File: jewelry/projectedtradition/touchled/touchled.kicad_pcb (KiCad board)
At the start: 2 copper layers, 22 x 22 mm, 10 parts, among them J1 Conn_01x01, J2 Conn_01x01, J3 Conn_01x01, J4 Conn_01x01, U1 TPP223-BA6

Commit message: jewelry: Initial layout for touchled
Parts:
- removed D1: LED, LEDs:LED_1206_HandSoldering
- removed J4: Conn_01x01, Pin_Headers:Pin_Header_Straight_1x01_Pitch1.27mm
- added C3: 1uF, Capacitors_SMD:C_0805_HandSoldering, F.Cu at (-9.14, 2.79)
- added C4: 1uF, Capacitors_SMD:C_0805_HandSoldering, F.Cu at (-0.25, -10.9)
- added TP1: TEST, touchuc:progpin, F.Cu at (10.7, -2.29)
- added TP2: TEST, touchuc:progpin, F.Cu at (-6.60, -9.14)
- added TP3: TEST, touchuc:progpin, F.Cu at (4.06, -6.60)
- added U2: AP3019A, touchled:SOT-223-6-extraspace, F.Cu at (-0.25, -7.62)
- BT1: footprint touchflower:BK-913 -> touchled:BK-913
- C1: value C -> 47pF
- C2: value CP -> 1uF; footprint Capacitors_SMD:C_1206_HandSoldering -> Capacitors_SMD:C_0805_HandSoldering
- R1: value R -> 22R
- U1: footprint touchflower:SOT-223-6-extraspace -> touchled:SOT-223-6-extraspace
- moved J3 12.4 mm to (-7.37, 5.84)
- moved R1 12.2 mm to (-7.62, -6.02), turned to 90 degrees
- moved U1 6.82 mm to (0.25, 8.96)
- moved C2 6.02 mm to (9.14, 2.79)
- moved J2 3.81 mm to (-4.32, -4.06)
- moved C1 3.17 mm to (-4.32, 7.87), turned to 90 degrees
- moved J1 3.06 mm to (4.32, -4.06)
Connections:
- J1 pad 1: VDD -> /LED+
- J2 pad 1: GND -> /LED-
- R1 pad 1: Net-(D1-Pad1) -> /LED-
- U1 pad 1: /out -> touchon
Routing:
- net /sensor: track 29.2 -> 0.00 mm
- net GND: track 23.6 -> 0.00 mm, vias 2 -> 0
- net /out: track 17.7 -> 0.00 mm
- net VDD: track 19.5 -> 6.52 mm
- net Net-(D1-Pad1): track 4.70 -> 0.00 mm
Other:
- board size 22 x 22 mm -> 24 x 24 mm

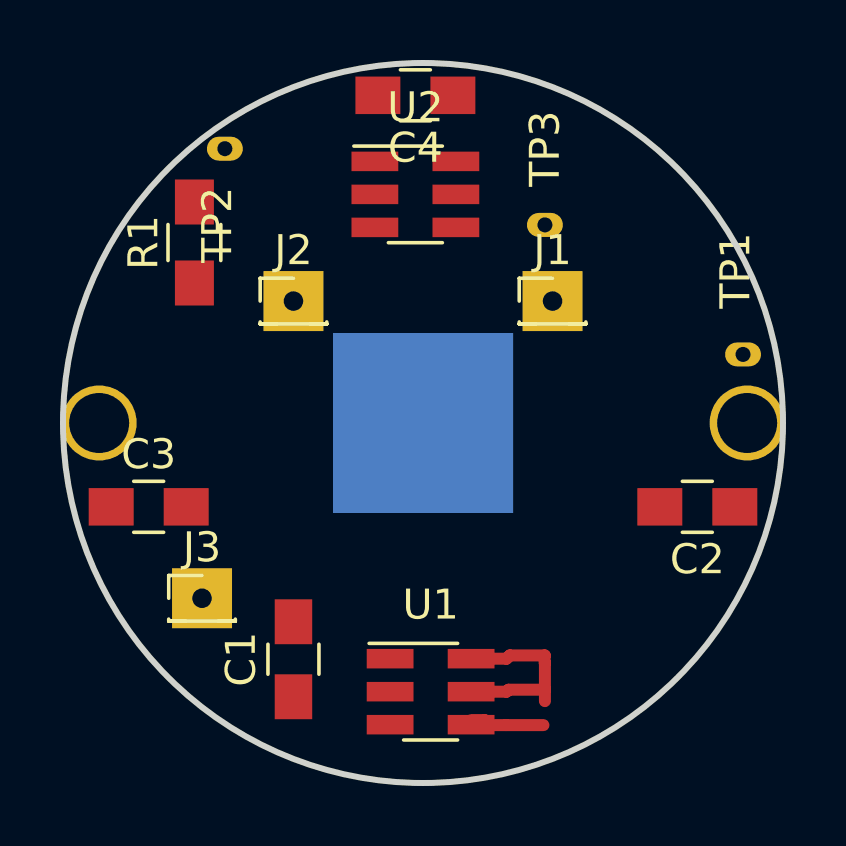
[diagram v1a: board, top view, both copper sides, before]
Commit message: jewelry: Complete initial LED driver layout
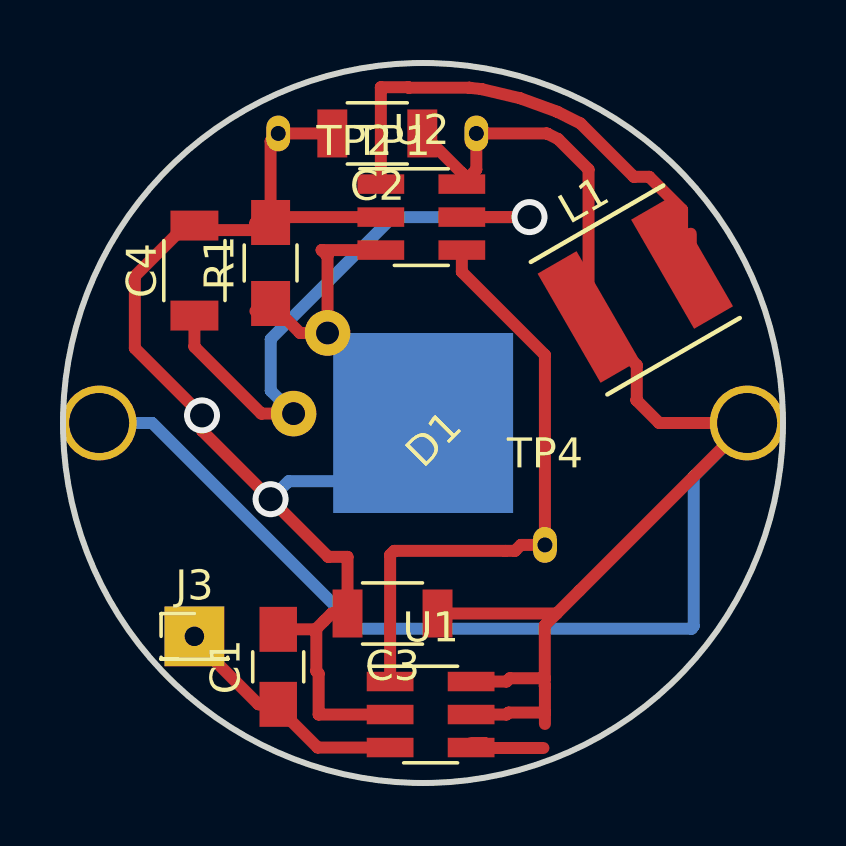
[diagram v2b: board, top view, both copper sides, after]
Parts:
- removed J1, J2: Conn_01x01, Pin_Headers:Pin_Header_Straight_1x01_Pitch1.27mm
- removed TP3: TEST, touchuc:progpin
- added D1: LED_Series, touchled:SIDELEDS1, F.Cu at (0.00, 0.18)
- added L1: L, Inductors:Inductor_Taiyo-Yuden_NR-50xx, F.Cu at (7.08, -4.43)
- added TP4: TEST, touchuc:progpin, F.Cu at (4.06, 4.06)
- C2, C3, C4: footprint Capacitors_SMD:C_0805_HandSoldering -> Capacitors_SMD:C_1206
- moved C2 16.4 mm to (-1.52, -9.65)
- moved TP1 11.5 mm to (1.78, -9.65), turned to 180 degrees
- moved C4 9.40 mm to (-7.62, -5.08), turned to 90 degrees
- moved C3 8.87 mm to (-1.02, 6.35), turned to 180 degrees
- moved R1 2.63 mm to (-5.08, -5.33)
- moved TP2 1.85 mm to (-4.83, -9.65), turned to 180 degrees
- moved J3 1.30 mm to (-7.62, 7.11)
- moved U2 0.78 mm to (-0.06, -6.86)
- moved U1 0.76 mm to (0.25, 9.72)
- moved C1 0.57 mm to (-4.83, 8.13)
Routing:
- net VDD: track 6.52 -> 72.9 mm
- net GND: track 0.00 -> 43.7 mm, vias 0 -> 2
- net /LED+: track 0.00 -> 20.6 mm, vias 0 -> 1
- net touchon: track 0.00 -> 20.6 mm
- net Net-(L1-Pad2): track 0.00 -> 18.5 mm
- net /sensor: track 0.00 -> 7.72 mm
- net /LED-: track 0.00 -> 7.53 mm

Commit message: jewelry: New PCB ready for test
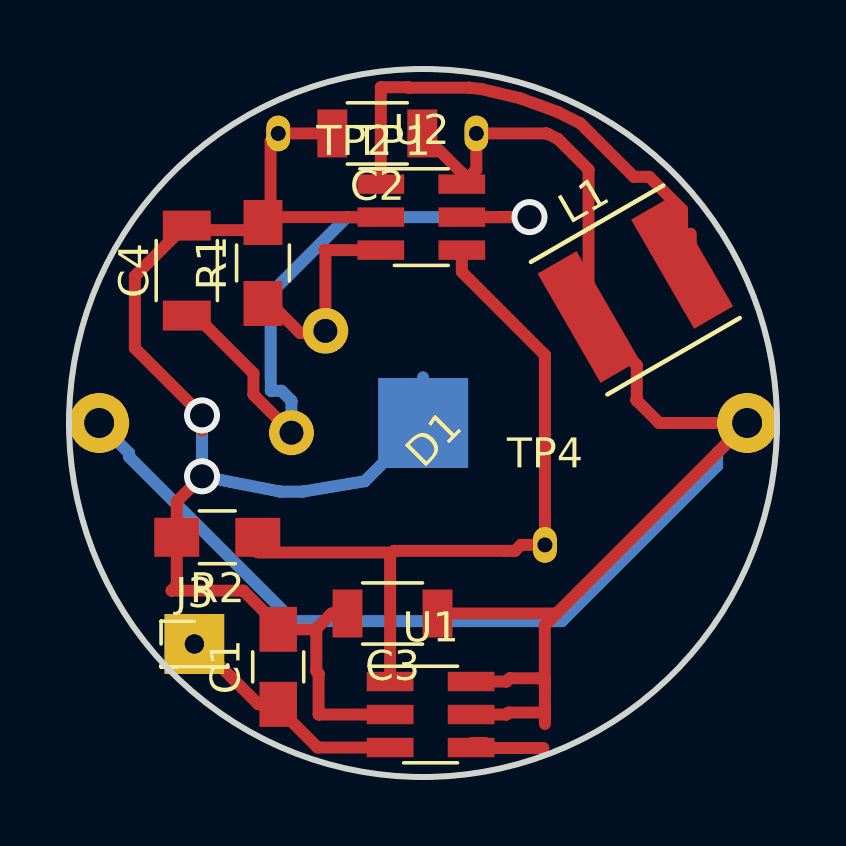
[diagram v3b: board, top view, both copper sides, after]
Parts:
- added R2: 10k, Resistors_SMD:R_0805_HandSoldering, F.Cu at (-6.86, 3.81)
- BT1: value Battery_Cell -> CR2032
- D1: value LED_Series -> LEDS
- J3: value Conn_01x01 -> SENSE
- R1: value 22R -> 47R
- TP1: value TEST -> VDD
- TP2: value TEST -> GND
- TP4: value TEST -> ON
- moved C4 0.25 mm to (-7.87, -5.08)
- moved J3 0.25 mm to (-7.62, 7.37)
- moved R1 0.25 mm to (-5.33, -5.33)
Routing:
- net touchon: track 20.6 -> 25.2 mm
- net GND: track 43.7 -> 47.8 mm
- net VDD: track 72.9 -> 70.1 mm
- net /LED+: track 20.6 -> 22.6 mm
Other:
- board size 24 x 24 mm -> 23.6 x 23.6 mm

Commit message: jewerly: Milled PCB
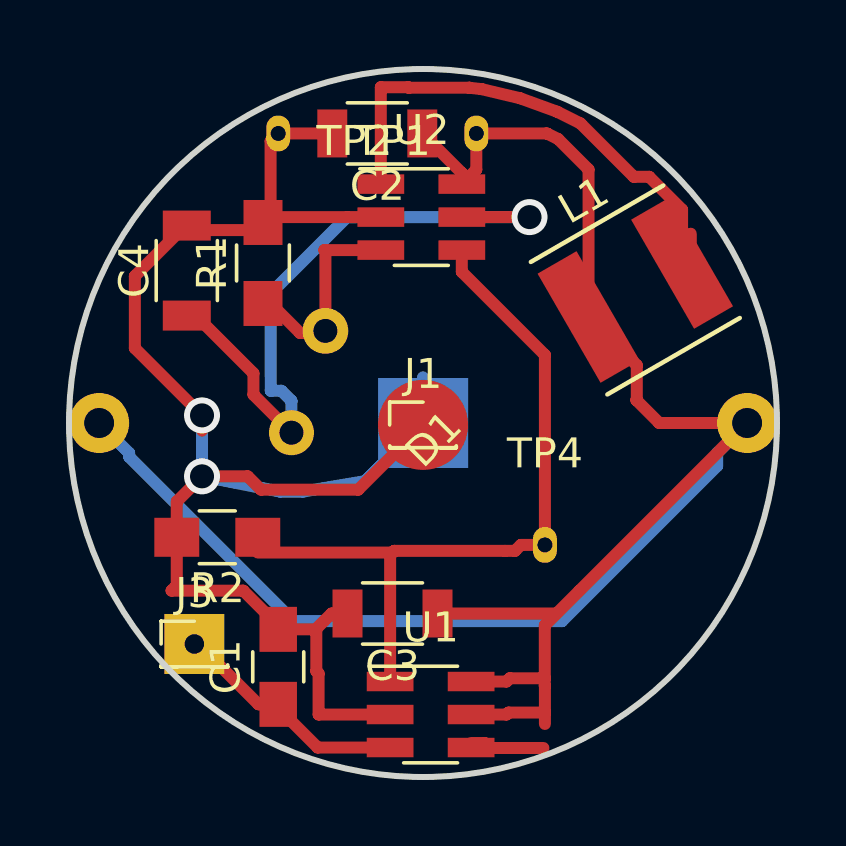
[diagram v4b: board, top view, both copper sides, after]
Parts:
- added J1: SENSEGND, Pin_Headers:Pin_Header_Straight_1x01_Pitch1.27mm, F.Cu at (0.00, 0.06)
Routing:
- net GND: track 47.8 -> 56.2 mm
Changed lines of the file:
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@@
     (thickness 1.6)
     (drawings 1)
-    (tracks 129)
+    (tracks 133)
     (zones 0)
-    (modules 15)
+    (modules 16)
     (nets 9)
   )
@@
     (mod_text_size 1 1)
     (mod_text_width 0.15)
-    (pad_size 2 2)
-    (pad_drill 0.65)
+    (pad_size 3 3)
+    (pad_drill 0)
     (pad_to_mask_clearance 0.2)
     (aux_axis_origin 0 0)
@@
       (net 1 GND))
     (model ${KISYS3DMOD}/Resistors_SMD.3dshapes/R_0805.wrl
+      (at (xyz 0 0 0))
+      (scale (xyz 1 1 1))
+      (rotate (xyz 0 0 0))
+    )
+  )
+  (module Pin_Headers:Pin_Header_Straight_1x01_Pitch1.27mm (layer F.Cu)
+    (at 0 0.0635)
+    (descr "Through hole straight pin header, 1x01, 1.27mm pitch, single row")
+    (tags "Through hole pin header THT 1x01 1.27mm single row")
+    (attr smd)
+    (fp_text reference J1 (at 0 -1.695) (layer F.SilkS)
+      (effects (font (size 1 1) (thickness 0.15)))
+    )
+    (fp_text value SENSEGND (at 0 1.695) (layer F.Fab)
+      (effects (font (size 1 1) (thickness 0.15)))
+    )
+    (fp_line (start -0.525 -0.635) (end 1.05 -0.635) (layer F.Fab) (width 0.1))
+    (fp_line (start 1.05 -0.635) (end 1.05 0.635) (layer F.Fab) (width 0.1))
+    (fp_line (start 1.05 0.635) (end -1.05 0.635) (layer F.Fab) (width 0.1))
+    (fp_line (start -1.05 0.635) (end -1.05 -0.11) (layer F.Fab) (width 0.1))
+    (fp_line (start -1.05 -0.11) (end -0.525 -0.635) (layer F.Fab) (width 0.1))
+    (fp_line (start -1.11 0.76) (end 1.11 0.76) (layer F.SilkS) (width 0.12))
+    (fp_line (start -1.11 0.76) (end -1.11 0.695) (layer F.SilkS) (width 0.12))
+    (fp_line (start 1.11 0.76) (end 1.11 0.695) (layer F.SilkS) (width 0.12))
+    (fp_line (start -1.11 0.76) (end -0.563471 0.76) (layer F.SilkS) (width 0.12))
+    (fp_line (start 0.563471 0.76) (end 1.11 0.76) (layer F.SilkS) (width 0.12))
+    (fp_line (start -1.11 0) (end -1.11 -0.76) (layer F.SilkS) (width 0.12))
+    (fp_line (start -1.11 -0.76) (end 0 -0.76) (layer F.SilkS) (width 0.12))
+    (fp_line (start -1.55 -1.15) (end -1.55 1.15) (layer F.CrtYd) (width 0.05))
+    (fp_line (start -1.55 1.15) (end 1.55 1.15) (layer F.CrtYd) (width 0.05))
+    (fp_line (start 1.55 1.15) (end 1.55 -1.15) (layer F.CrtYd) (width 0.05))
+    (fp_line (start 1.55 -1.15) (end -1.55 -1.15) (layer F.CrtYd) (width 0.05))
+    (fp_text user %R (at 0 0 90) (layer F.Fab)
+      (effects (font (size 1 1) (thickness 0.15)))
+    )
+    (pad 1 smd circle (at 0 0) (size 3 3) (layers F.Cu F.Paste F.Mask)
+      (net 1 GND))
+    (model ${KISYS3DMOD}/Pin_Headers.3dshapes/Pin_Header_Straight_1x01_Pitch1.27mm.wrl
       (at (xyz 0 0 0))
       (scale (xyz 1 1 1))
@@
   (segment (start -1.935001 1.940001) (end -4.0005 2.286) (width 0.4) (layer B.Cu) (net 1))
   (segment (start -7.366 1.778) (end -7.366 -0.254) (width 0.4) (layer B.Cu) (net 1))
+  (segment (start -7.366 1.778) (end -5.842 1.778) (width 0.4) (layer F.Cu) (net 1))
+  (segment (start -5.842 1.778) (end -5.3975 2.2225) (width 0.4) (layer F.Cu) (net 1))
+  (segment (start -2.159 2.2225) (end 0 0.0635) (width 0.4) (layer F.Cu) (net 1))
+  (segment (start -5.3975 2.2225) (end -2.159 2.2225) (width 0.4) (layer F.Cu) (net 1))
   (segment (start 2.059 10.668) (end 2.22401 10.83301) (width 0.4) (layer F.Cu) (net 2))
   (segment (start 1.604 10.668) (end 2.059 10.668) (width 0.4) (layer F.Cu) (net 2))

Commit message: jewelry: Fixed one missing trace
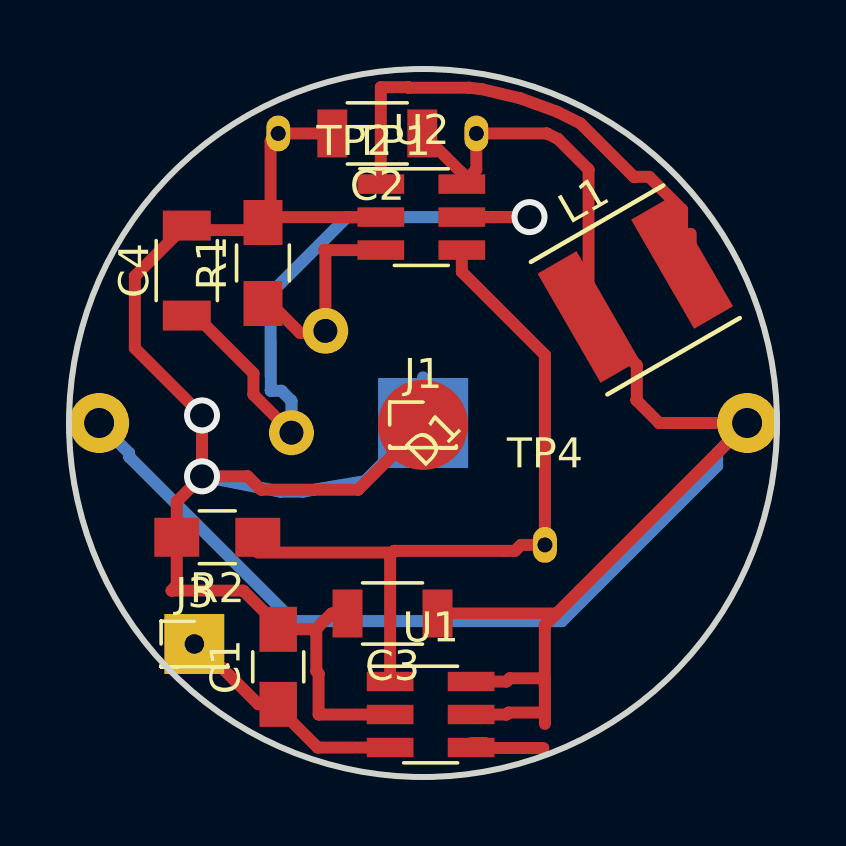
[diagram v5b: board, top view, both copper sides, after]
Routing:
- net GND: track 56.2 -> 55.7 mm
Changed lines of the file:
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@@
     (thickness 1.6)
     (drawings 1)
-    (tracks 133)
+    (tracks 132)
     (zones 0)
     (modules 16)
@@
   (segment (start -9.60535 -4.89465) (end -7.92 -6.58) (width 0.4) (layer F.Cu) (net 1))
   (segment (start -9.60535 -2.49335) (end -9.60535 -4.89465) (width 0.4) (layer F.Cu) (net 1))
-  (segment (start -7.366 -0.254) (end -7.366 0.254) (width 0.4) (layer F.Cu) (net 1))
   (segment (start -3.048 6.35) (end -3.302 6.604) (width 0.4) (layer F.Cu) (net 1))
   (segment (start -2.516 6.35) (end -3.048 6.35) (width 0.4) (layer F.Cu) (net 1))
@@
   (segment (start 0.005 0) (end -1.935001 1.940001) (width 0.4) (layer B.Cu) (net 1))
   (segment (start -1.935001 1.940001) (end -4.0005 2.286) (width 0.4) (layer B.Cu) (net 1))
-  (segment (start -7.366 1.778) (end -7.366 -0.254) (width 0.4) (layer B.Cu) (net 1))
   (segment (start -7.366 1.778) (end -5.842 1.778) (width 0.4) (layer F.Cu) (net 1))
   (segment (start -5.842 1.778) (end -5.3975 2.2225) (width 0.4) (layer F.Cu) (net 1))
   (segment (start -2.159 2.2225) (end 0 0.0635) (width 0.4) (layer F.Cu) (net 1))
   (segment (start -5.3975 2.2225) (end -2.159 2.2225) (width 0.4) (layer F.Cu) (net 1))
+  (segment (start -7.366 -0.254) (end -7.366 1.778) (width 0.4) (layer F.Cu) (net 1))
   (segment (start 2.059 10.668) (end 2.22401 10.83301) (width 0.4) (layer F.Cu) (net 2))
   (segment (start 1.604 10.668) (end 2.059 10.668) (width 0.4) (layer F.Cu) (net 2))

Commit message: jewelry: Back to single LED
NMOS switch to avoid LED on when off
Smaller inductor
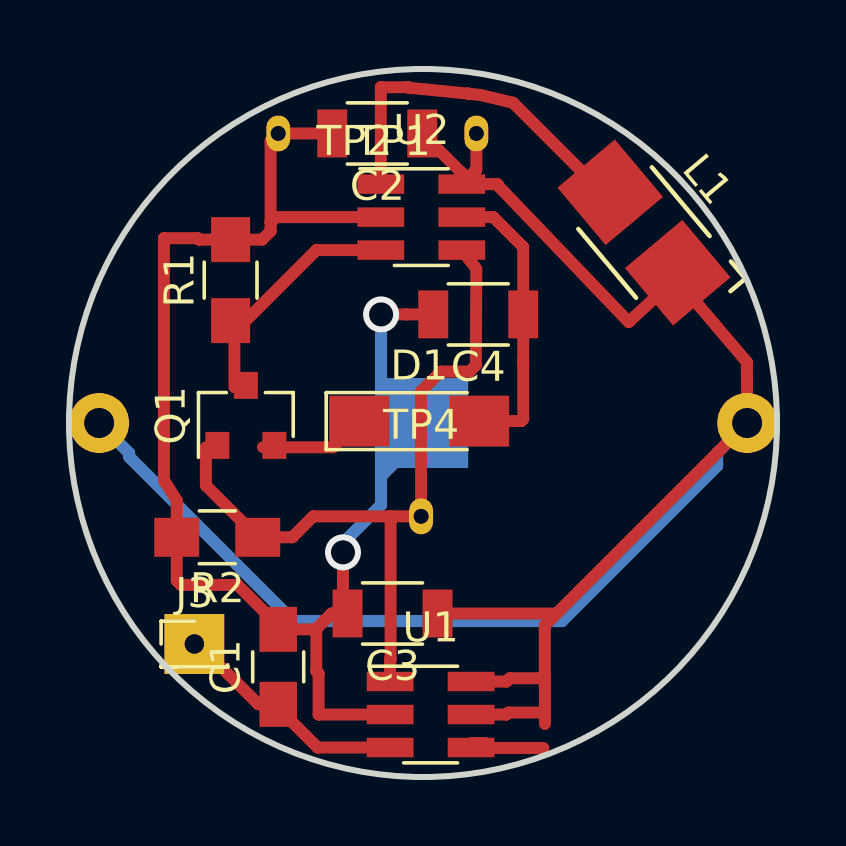
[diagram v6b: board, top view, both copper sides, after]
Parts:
- removed J1: SENSEGND, Pin_Headers:Pin_Header_Straight_1x01_Pitch1.27mm
- added Q1: Q_NMOS_GSD, TO_SOT_Packages_SMD:SOT-23, F.Cu at (-5.91, -0.25)
- D1: value LEDS -> LED; footprint touchled:SIDELEDS1 -> LEDs:LED_1206_HandSoldering
- L1: footprint Inductors:Inductor_Taiyo-Yuden_NR-50xx -> Inductors:Inductor_1212
- R1: value 47R -> 12R
- R2: value 10k -> 100k
- moved C4 9.82 mm to (1.84, -3.62), turned to 180 degrees
- moved TP4 4.24 mm to (-0.06, 3.11)
- moved L1 1.94 mm to (7.37, -6.35), turned to 130 degrees
- moved R1 1.22 mm to (-6.41, -4.76)
- moved D1 0.28 mm to (-0.13, -0.06), turned to 0 degrees
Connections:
- R1 pad 1: /LED- -> Net-(Q1-Pad3)
- U2 pad 3: /LED- -> Net-(Q1-Pad3)
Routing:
- net /LED+: track 22.6 -> 9.69 mm, vias 1 -> 0
- net Net-(Q1-Pad3): track 0.00 -> 8.39 mm
- net Net-(L1-Pad2): track 18.5 -> 12.6 mm
- net GND: track 55.7 -> 50.7 mm
- net /LED-: track 7.30 -> 3.57 mm
- net VDD: track 70.1 -> 68.9 mm

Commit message: jewelry: Add reverse polarity protection
Needed one 0 ohm resistor
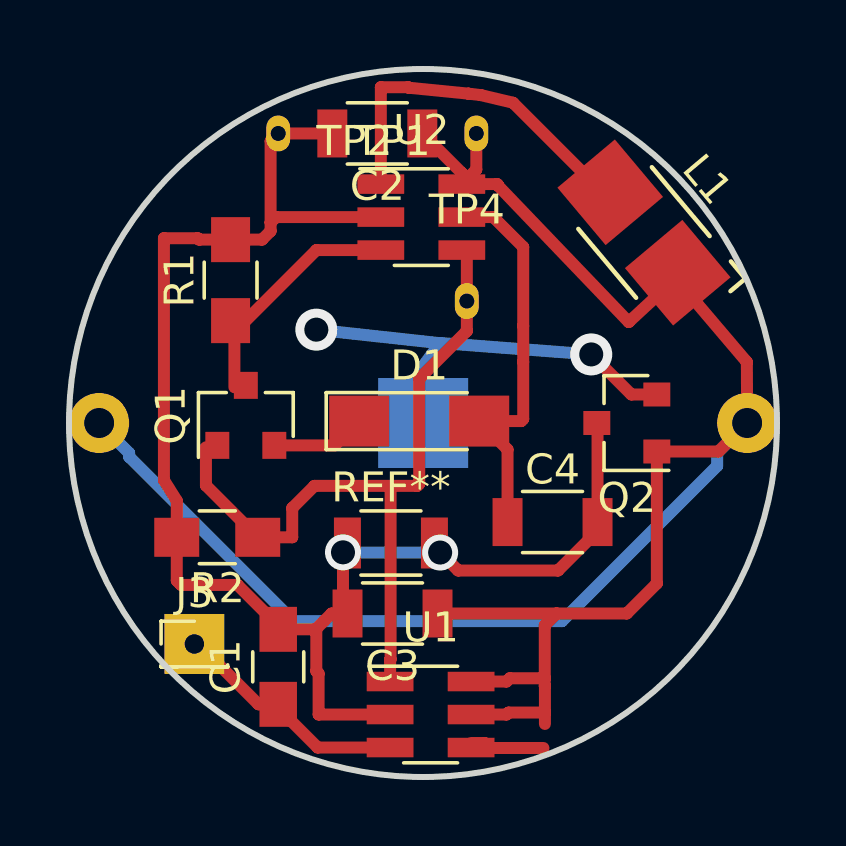
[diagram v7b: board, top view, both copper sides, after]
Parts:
- added Q2: Q_NMOS_GSD, TO_SOT_Packages_SMD:SOT-23, F.Cu at (6.79, 0.00)
- added REF**: R_1206, Resistors_SMD:R_1206, F.Cu at (-1.07, 4.00)
- moved C4 7.35 mm to (4.32, 3.30), turned to 0 degrees
- moved TP4 7.34 mm to (1.46, -4.06)
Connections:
- BT1 pad 2: GND -> Net-(BT1-Pad2)
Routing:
- net Net-(BT1-Pad2): track 0.00 -> 15.1 mm, vias 0 -> 2
- net /LED+: track 9.69 -> 13.7 mm
- net VDD: track 68.9 -> 71.5 mm
- net GND: track 50.7 -> 51.4 mm
